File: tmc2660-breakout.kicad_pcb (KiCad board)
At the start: 2 copper layers, 15 parts, among them P1 CONN_01X04, P2 CONN_01X02, P3 CONN_01X04, U1 TMC2660

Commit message: o little tweaks.
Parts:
- moved P2 32.5 mm to (130.8, 44.5), turned to 270 degrees
- moved P3 30.2 mm to (125.7, 38.1), turned to 90 degrees
- moved P1 24.7 mm to (133.3, 76.2), turned to 270 degrees
- moved C1 23.1 mm to (125.5, 66.0)
- moved R5 21.7 mm to (142.2, 54.6)
- moved C5 12.9 mm to (118.1, 62.2), turned to 270 degrees
- moved C4 5.35 mm to (141.0, 61.0)
- moved U1 0.90 mm to (129.6, 54.6)
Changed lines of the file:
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@@
-(kicad_pcb (version 4) (host pcbnew "(after 2015-may-25 BZR unknown)-product")
+(kicad_pcb (version 4) (host pcbnew "(2015-08-05 BZR 6054, Git 5c8efeb)-product")
   (general
     (links 47)
     (no_connects 47)
-    (area 0 0 0 0)
+    (area 122.428 46.736 168.09492 70.836)
     (thickness 1.6)
     (drawings 0)
@@
   )
   (module Resistors_SMD:R_1206 (layer F.Cu)
-    (at 124.853001 67.561)
+    (at 142.24 54.61)
     (descr "Resistor SMD 1206, reflow soldering, Vishay (see dcrcw.pdf)")
     (tags "resistor 1206")
@@
   )
   (module Capacitors_SMD:C_0805 (layer F.Cu)
-    (at 148.603001 65.811)
+    (at 125.46 66.04)
     (descr "Capacitor SMD 0805, reflow soldering, AVX (see smccp.pdf)")
     (tags "capacitor 0805")
@@
   )
   (module Capacitors_SMD:C_1206 (layer F.Cu)
-    (at 139.203001 66.011)
+    (at 140.97 60.96)
     (descr "Capacitor SMD 1206, reflow soldering, AVX (see smccp.pdf)")
     (tags "capacitor 1206")
@@
   )
   (module Capacitors_SMD:C_1206 (layer F.Cu)
-    (at 129.803001 67.561)
+    (at 118.11 62.23 270)
     (descr "Capacitor SMD 1206, reflow soldering, AVX (see smccp.pdf)")
     (tags "capacitor 1206")
     (attr smd)
-    (fp_text reference C5 (at 0 -2.3) (layer F.SilkS)
-      (effects (font (size 1 1) (thickness 0.15)))
-    )
-    (fp_text value CP (at 0 2.3) (layer F.Fab)
+    (fp_text reference C5 (at 0 -2.3 270) (layer F.SilkS)
+      (effects (font (size 1 1) (thickness 0.15)))
+    )
+    (fp_text value CP (at 0 2.3 270) (layer F.Fab)
       (effects (font (size 1 1) (thickness 0.15)))
     )
@@
     (fp_line (start 1 -1.025) (end -1 -1.025) (layer F.SilkS) (width 0.15))
     (fp_line (start -1 1.025) (end 1 1.025) (layer F.SilkS) (width 0.15))
-    (pad 1 smd rect (at -1.5 0) (size 1 1.6) (layers F.Cu F.Paste F.Mask)
+    (pad 1 smd rect (at -1.5 0 270) (size 1 1.6) (layers F.Cu F.Paste F.Mask)
       (net 9 VMot))
-    (pad 2 smd rect (at 1.5 0) (size 1 1.6) (layers F.Cu F.Paste F.Mask)
+    (pad 2 smd rect (at 1.5 0 270) (size 1 1.6) (layers F.Cu F.Paste F.Mask)
       (net 7 GND))
     (model Capacitors_SMD.3dshapes/C_1206.wrl
@@
   )
   (module Pin_Headers:Pin_Header_Straight_1x04 (layer F.Cu)
-    (at 141.786333 52.961)
+    (at 133.35 76.2 270)
     (descr "Through hole pin header")
     (tags "pin header")
-    (fp_text reference P1 (at 0 -5.1) (layer F.SilkS)
-      (effects (font (size 1 1) (thickness 0.15)))
-    )
-    (fp_text value CONN_01X04 (at 0 -3.1) (layer F.Fab)
+    (fp_text reference P1 (at 0 -5.1 270) (layer F.SilkS)
+      (effects (font (size 1 1) (thickness 0.15)))
+    )
+    (fp_text value CONN_01X04 (at 0 -3.1 270) (layer F.Fab)
       (effects (font (size 1 1) (thickness 0.15)))
     )
@@
     (fp_line (start -1.55 0) (end -1.55 -1.55) (layer F.SilkS) (width 0.15))
     (fp_line (start -1.55 -1.55) (end 1.55 -1.55) (layer F.SilkS) (width 0.15))
-    (pad 1 thru_hole rect (at 0 0) (size 2.032 1.7272) (drill 1.016) (layers *.Cu *.Mask F.SilkS)
+    (pad 1 thru_hole rect (at 0 0 270) (size 2.032 1.7272) (drill 1.016) (layers *.Cu *.Mask F.SilkS)
       (net 11 "Net-(P1-Pad1)"))
-    (pad 2 thru_hole oval (at 0 2.54) (size 2.032 1.7272) (drill 1.016) (layers *.Cu *.Mask F.SilkS)
+    (pad 2 thru_hole oval (at 0 2.54 270) (size 2.032 1.7272) (drill 1.016) (layers *.Cu *.Mask F.SilkS)
       (net 12 "Net-(P1-Pad2)"))
-    (pad 3 thru_hole oval (at 0 5.08) (size 2.032 1.7272) (drill 1.016) (layers *.Cu *.Mask F.SilkS)
+    (pad 3 thru_hole oval (at 0 5.08 270) (size 2.032 1.7272) (drill 1.016) (layers *.Cu *.Mask F.SilkS)
       (net 13 "Net-(P1-Pad3)"))
-    (pad 4 thru_hole oval (at 0 7.62) (size 2.032 1.7272) (drill 1.016) (layers *.Cu *.Mask F.SilkS)
+    (pad 4 thru_hole oval (at 0 7.62 270) (size 2.032 1.7272) (drill 1.016) (layers *.Cu *.Mask F.SilkS)
       (net 14 "Net-(P1-Pad4)"))
     (model Pin_Headers.3dshapes/Pin_Header_Straight_1x04.wrl
@@
   )
   (module Pin_Headers:Pin_Header_Straight_1x02 (layer F.Cu)
-    (at 162.206333 52.961)
+    (at 130.81 44.45 270)
     (descr "Through hole pin header")
     (tags "pin header")
-    (fp_text reference P2 (at 0 -5.1) (layer F.SilkS)
-      (effects (font (size 1 1) (thickness 0.15)))
-    )
-    (fp_text value CONN_01X02 (at 0 -3.1) (layer F.Fab)
+    (fp_text reference P2 (at 0 -5.1 270) (layer F.SilkS)
+      (effects (font (size 1 1) (thickness 0.15)))
+    )
+    (fp_text value CONN_01X02 (at 0 -3.1 270) (layer F.Fab)
       (effects (font (size 1 1) (thickness 0.15)))
     )
@@
     (fp_line (start -1.27 1.27) (end -1.27 3.81) (layer F.SilkS) (width 0.15))
     (fp_line (start -1.27 3.81) (end 1.27 3.81) (layer F.SilkS) (width 0.15))
-    (pad 1 thru_hole rect (at 0 0) (size 2.032 2.032) (drill 1.016) (layers *.Cu *.Mask F.SilkS)
+    (pad 1 thru_hole rect (at 0 0 270) (size 2.032 2.032) (drill 1.016) (layers *.Cu *.Mask F.SilkS)
       (net 15 "Net-(P2-Pad1)"))
-    (pad 2 thru_hole oval (at 0 2.54) (size 2.032 2.032) (drill 1.016) (layers *.Cu *.Mask F.SilkS)
+    (pad 2 thru_hole oval (at 0 2.54 270) (size 2.032 2.032) (drill 1.016) (layers *.Cu *.Mask F.SilkS)
       (net 16 "Net-(P2-Pad2)"))
     (model Pin_Headers.3dshapes/Pin_Header_Straight_1x02.wrl
@@
   )
   (module Pin_Headers:Pin_Header_Straight_1x04 (layer F.Cu)
-    (at 151.996333 52.961)
+    (at 125.73 38.1 90)
     (descr "Through hole pin header")
     (tags "pin header")
-    (fp_text reference P3 (at 0 -5.1) (layer F.SilkS)
-      (effects (font (size 1 1) (thickness 0.15)))
-    )
-    (fp_text value CONN_01X04 (at 0 -3.1) (layer F.Fab)
+    (fp_text reference P3 (at 0 -5.1 90) (layer F.SilkS)
+      (effects (font (size 1 1) (thickness 0.15)))
+    )
+    (fp_text value CONN_01X04 (at 0 -3.1 90) (layer F.Fab)
       (effects (font (size 1 1) (thickness 0.15)))
     )
@@
     (fp_line (start -1.55 0) (end -1.55 -1.55) (layer F.SilkS) (width 0.15))
     (fp_line (start -1.55 -1.55) (end 1.55 -1.55) (layer F.SilkS) (width 0.15))
-    (pad 1 thru_hole rect (at 0 0) (size 2.032 1.7272) (drill 1.016) (layers *.Cu *.Mask F.SilkS)
+    (pad 1 thru_hole rect (at 0 0 90) (size 2.032 1.7272) (drill 1.016) (layers *.Cu *.Mask F.SilkS)
       (net 17 1A1))
-    (pad 2 thru_hole oval (at 0 2.54) (size 2.032 1.7272) (drill 1.016) (layers *.Cu *.Mask F.SilkS)
+    (pad 2 thru_hole oval (at 0 2.54 90) (size 2.032 1.7272) (drill 1.016) (layers *.Cu *.Mask F.SilkS)
       (net 18 1A2))
-    (pad 3 thru_hole oval (at 0 5.08) (size 2.032 1.7272) (drill 1.016) (layers *.Cu *.Mask F.SilkS)
+    (pad 3 thru_hole oval (at 0 5.08 90) (size 2.032 1.7272) (drill 1.016) (layers *.Cu *.Mask F.SilkS)
       (net 19 1B1))
-    (pad 4 thru_hole oval (at 0 7.62) (size 2.032 1.7272) (drill 1.016) (layers *.Cu *.Mask F.SilkS)
+    (pad 4 thru_hole oval (at 0 7.62 90) (size 2.032 1.7272) (drill 1.016) (layers *.Cu *.Mask F.SilkS)
       (net 20 1B2))
     (model Pin_Headers.3dshapes/Pin_Header_Straight_1x04.wrl
@@
   )
   (module Housings_QFP:LQFP-44_10x10mm_Pitch0.8mm (layer F.Cu)
-    (at 129.553001 55.511)
+    (at 129.553001 54.61)
     (descr "LQFP44 (see Appnote_PCB_Guidelines_TRINAMIC_packages.pdf)")
     (tags "QFP 0.8")

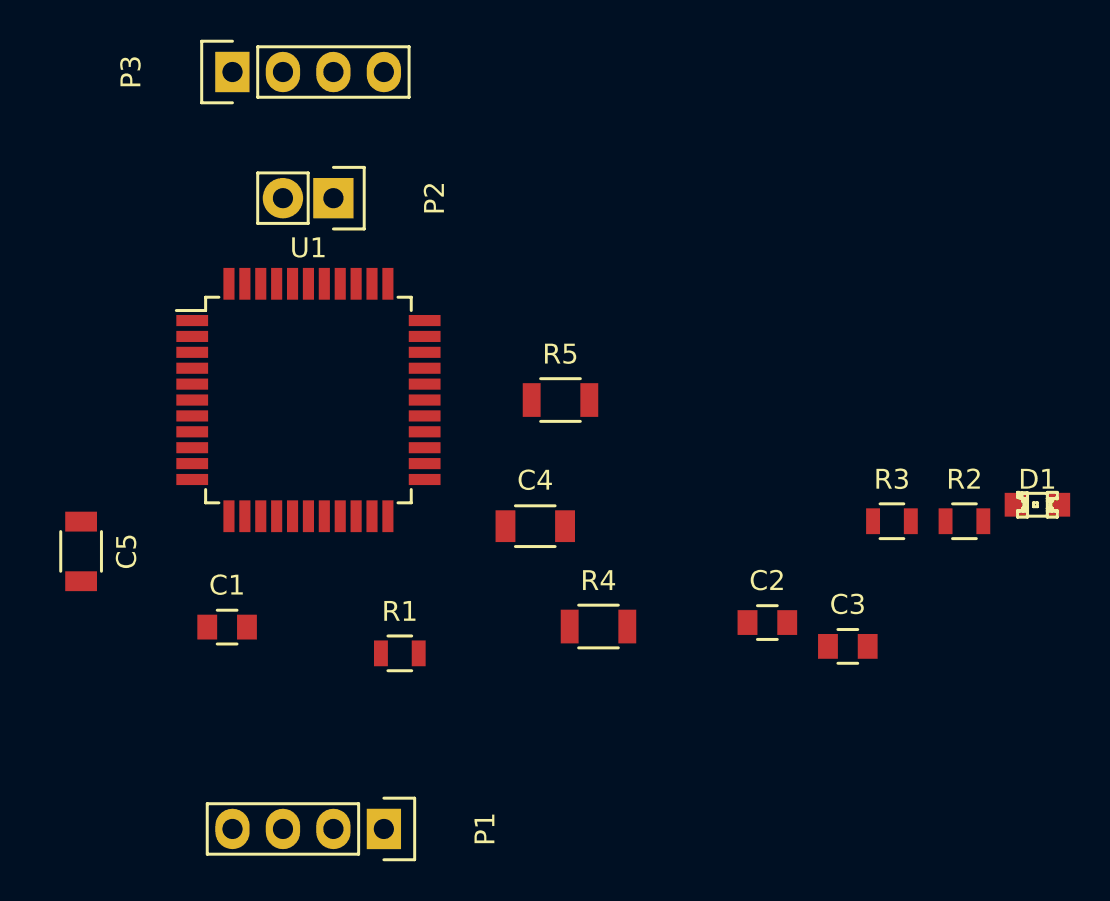
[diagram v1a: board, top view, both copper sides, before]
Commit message: o First fully placed and routed.
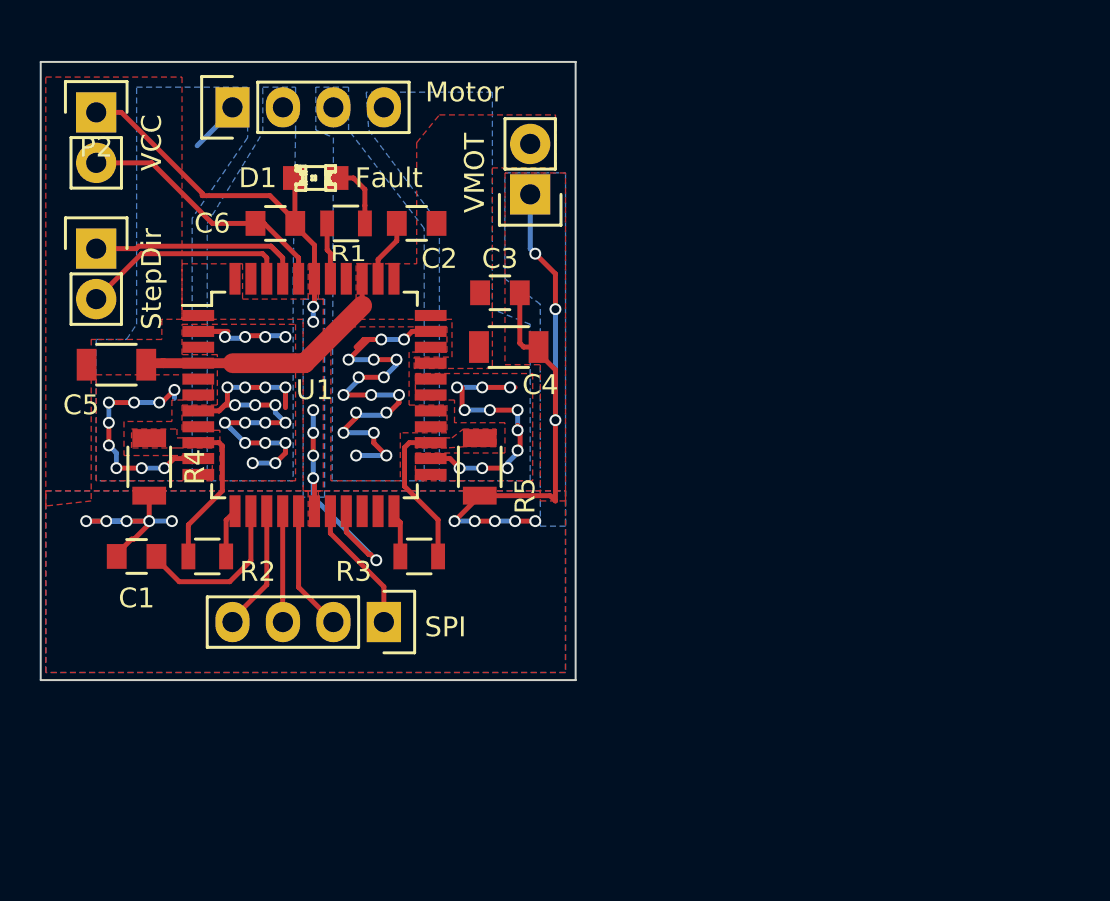
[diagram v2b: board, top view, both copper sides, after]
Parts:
- added C6: 100n, Capacitors_SMD:C_0805, F.Cu at (127.9, 45.7)
- added P4: VCC, Pin_Headers:Pin_Header_Straight_1x02, F.Cu at (118.9, 40.1)
- added P5: VMOT, Pin_Headers:Pin_Header_Straight_1x02, F.Cu at (140.7, 44.3)
- C1: value C -> 470n
- C2, C3: value C -> 100n
- C4, C5: value CP -> 10u
- P1: value CONN_01X04 -> SPI
- P2: value CONN_01X02 -> StepDir
- P3: value CONN_01X04 -> Motor
- R2, R3: value R -> 10k
- R4, R5: value R -> 0.075
- moved D1 39.9 mm to (129.9, 43.4)
- moved R2 38.2 mm to (124.5, 62.5)
- moved C2 26.7 mm to (135.0, 45.7), turned to 180 degrees
- moved C3 25.0 mm to (139.2, 49.2)
- moved R4 24.0 mm to (121.5, 58.0), turned to 270 degrees
- moved R3 23.9 mm to (135.1, 62.5), turned to 180 degrees
- moved R1 21.8 mm to (131.4, 45.7)
- moved P2 12.2 mm to (118.9, 47.0), turned to 0 degrees
- moved P1 10.4 mm to (133.3, 65.8)
- moved C5 9.56 mm to (119.9, 52.8), turned to 180 degrees
- moved C4 9.12 mm to (139.6, 51.9)
- moved C1 5.78 mm to (120.9, 62.5), turned to 180 degrees
- moved R5 5.28 mm to (138.2, 58.0), turned to 270 degrees
- moved P3 1.78 mm to (125.7, 39.9)
- moved U1 0.40 mm to (129.9, 54.4)
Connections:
- P3 pad 1: 1A1 -> 1A2
- P3 pad 2: 1A2 -> 1A1
- U1 pad 1: (no net) -> GND
- U1 pad 14: Net-(P1-Pad3) -> Net-(P1-Pad4)
- U1 pad 15: Net-(P1-Pad2) -> Net-(P1-Pad3)
- U1 pad 16: Net-(P1-Pad4) -> Net-(P1-Pad2)
- U1 pad 19: Net-(U1-Pad19) -> GND
- U1 pad 21: Net-(U1-Pad21) -> (no net)
- U1 pad 33: (no net) -> VMot
- U1 pad 40: +3V3 -> Net-(C6-Pad1)
- U1 pad 43: Net-(U1-Pad43) -> (no net)
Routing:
- net GND: track 0.00 -> 78.4 mm, vias 0 -> 20
- net 1A1: track 0.00 -> 25.4 mm, vias 0 -> 20
- net 1B1: track 0.00 -> 23.7 mm, vias 0 -> 16
- net 1A2: track 0.00 -> 14.4 mm, vias 0 -> 9
- net 1B2: track 0.00 -> 13.8 mm, vias 0 -> 11
- net VMot: track 0.00 -> 13.7 mm
- net Net-(C6-Pad1): track 0.00 -> 13.2 mm
- net Net-(P2-Pad1): track 0.00 -> 11.6 mm
- net Net-(P2-Pad2): track 0.00 -> 10.7 mm
- net Net-(C1-Pad1): track 0.00 -> 8.28 mm
- net Net-(R2-Pad1): track 0.00 -> 8.12 mm
- net Net-(R3-Pad1): track 0.00 -> 7.60 mm
- net Net-(P1-Pad1): track 0.00 -> 6.70 mm
- net Net-(P1-Pad2): track 0.00 -> 6.31 mm
- net Net-(P1-Pad4): track 0.00 -> 6.30 mm
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- added copper zone on B.Cu, net 1A1
- added copper zone on F.Cu, net 1A1
- added copper zone on B.Cu, net 1A2
- added copper zone on F.Cu, net 1A2
- added copper zone on B.Cu, net 1B1
- added copper zone on F.Cu, net 1B1
- added copper zone on B.Cu, net 1B2
- added copper zone on F.Cu, net 1B2
- added copper zone on B.Cu, net GND
- added copper zone on F.Cu, net GND
- added copper zone on F.Cu, net Net-(R2-Pad1)
- added copper zone on F.Cu, net Net-(R3-Pad1)
- added copper zone on F.Cu, net VMot
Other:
- board outline added: 26.9 x 31.1 mm
- net class Default: clearance 0.2 -> 0.127
- rule trace_clearance: 0.2 -> 0.127
- board text added: "Fault"
